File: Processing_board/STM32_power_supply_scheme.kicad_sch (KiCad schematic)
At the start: 14 parts

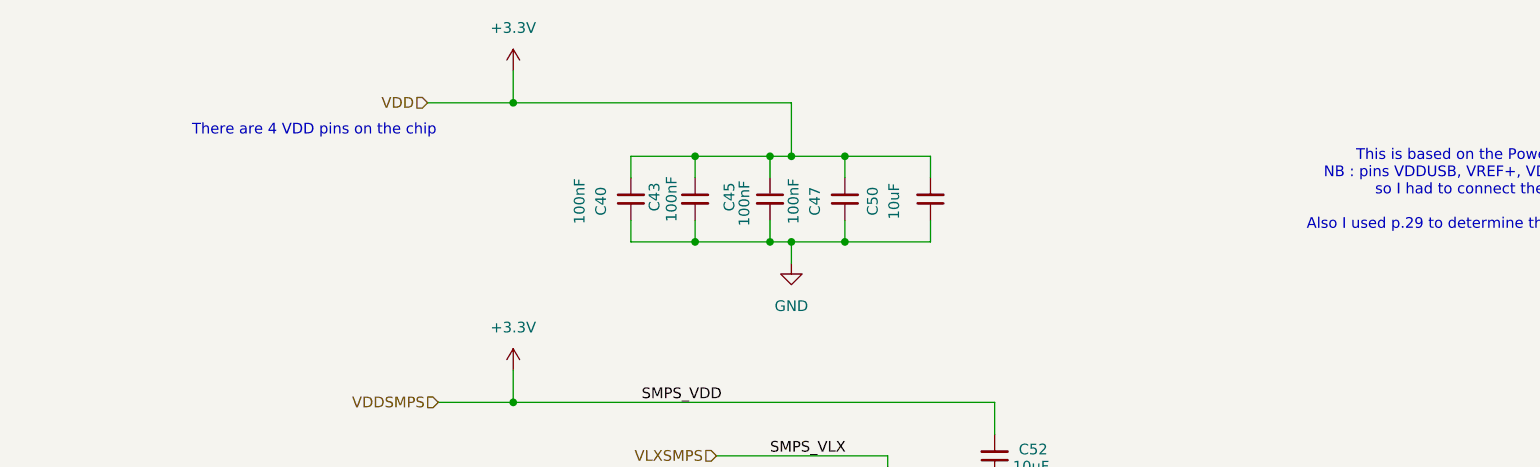
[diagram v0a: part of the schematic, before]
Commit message: created BOM, deleted useless folder Components and renamed CAD_Models to Parts
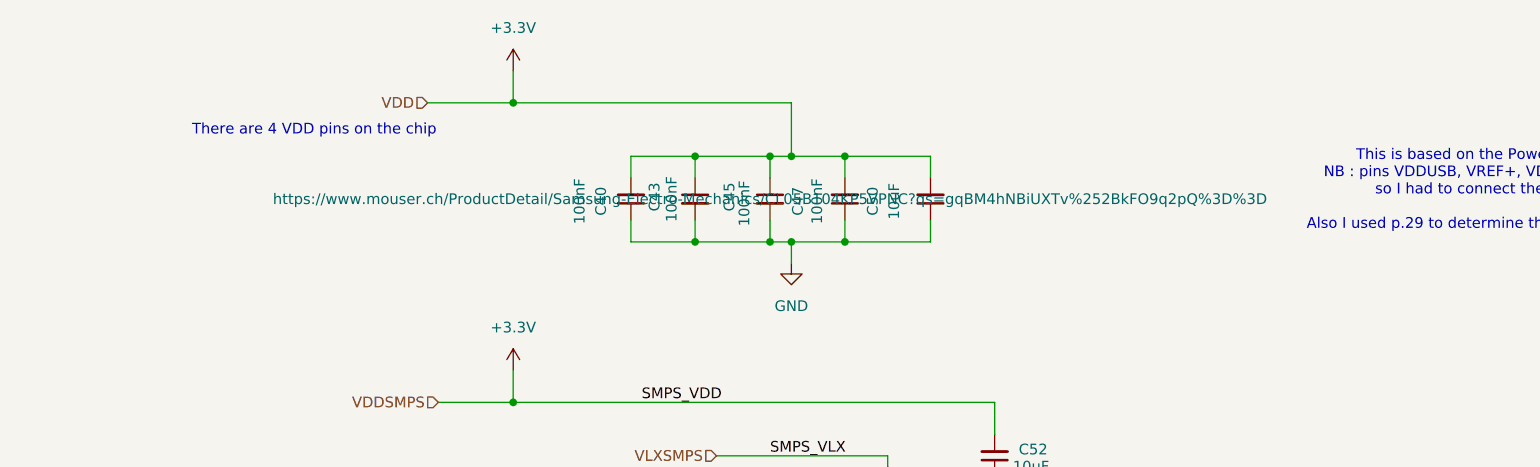
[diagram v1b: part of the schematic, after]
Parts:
- C40, C41, C42, C43, C45, C46, C47, C51: Link (none) -> https://www.mouser.ch/ProductDetail/Samsung-Electro-Mechani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; MANUFACTURER (none) -> Samsung Electro-Mechanics; Manufacturer_Part_Number (none) -> CL05B104KP5VPNC; Panier (none) -> 1
- C44: Link (none) -> https://www.mouser.ch/ProductDetail/Samsung-Electro-Mechani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; MANUFACTURER (none) -> Samsung Electro-Mechanics; Manufacturer_Part_Number (none) -> CL05A105KP5NNNC; Panier (none) -> 1
- C48: Link (none) -> https://www.mouser.ch/ProductDetail/KEMET/C0402C473K8RACAUT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; MANUFACTURER (none) -> KEMET; Manufacturer_Part_Number (none) -> C0402C473K8RACAUTO7411; Panier (none) -> 1
- C49: Link (none) -> https://www.mouser.ch/ProductDetail/YAGEO/CC0402KRX5R6BB475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; MANUFACTURER (none) -> YAGEO; Manufacturer_Part_Number (none) -> CC0402KRX5R6BB475; Panier (none) -> 1
- C50, C52: Link (none) -> https://www.mouser.ch/ProductDetail/Murata-Electronics/GRM1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; MANUFACTURER (none) -> Murata Electronics; Manufacturer_Part_Number (none) -> GRM155R61A106ME11D; Panier (none) -> 1
- L3: Link (none) -> https://www.mouser.ch/ProductDetail/Wurth-Elektronik/744797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; MANUFACTURER (none) -> Wurth Elektronik; Manufacturer_Part_Number (none) -> 74479774222; Panier (none) -> 1

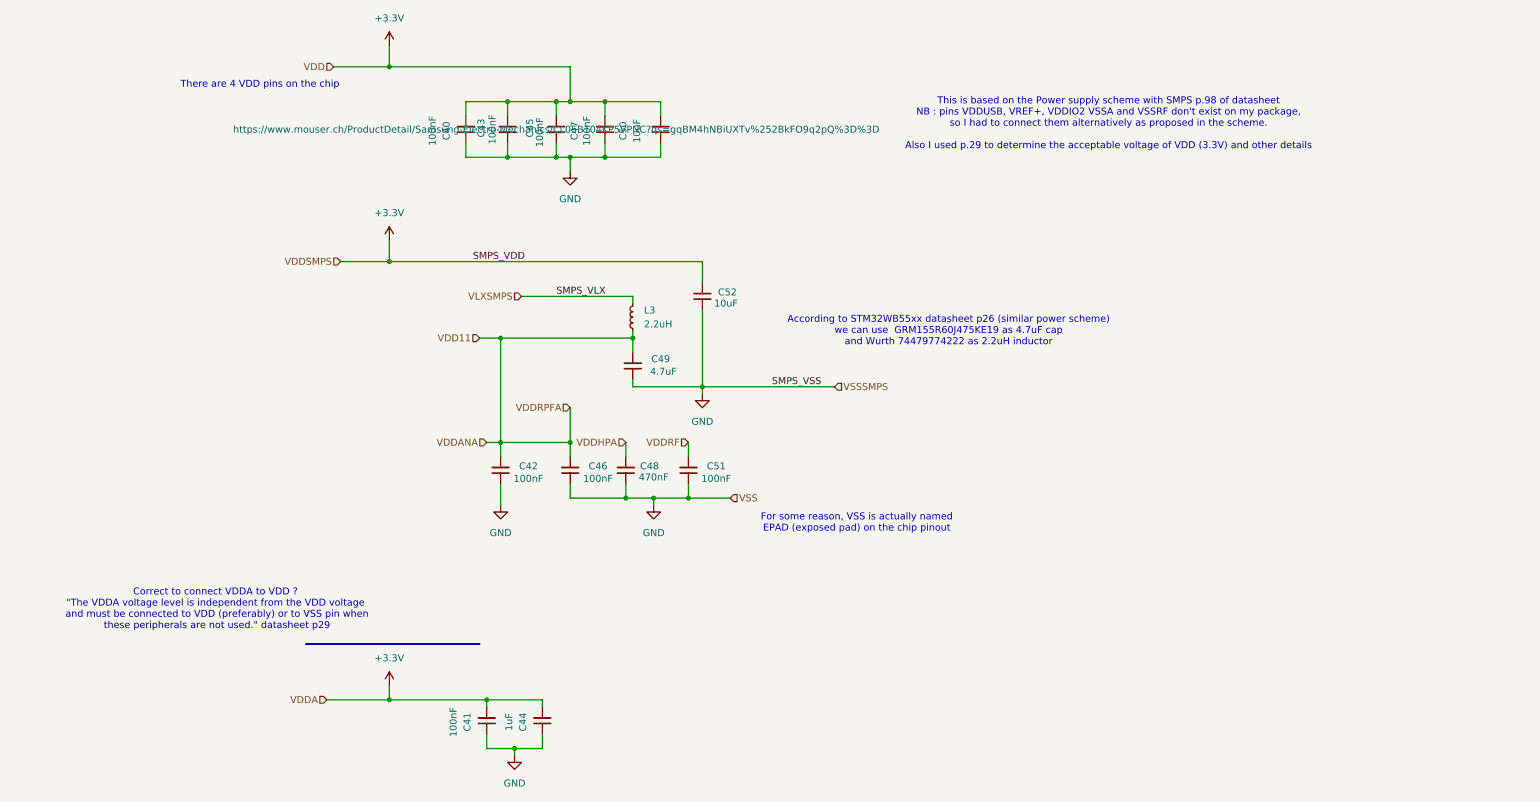
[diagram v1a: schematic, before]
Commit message: added N-Pulse logo etc, added open jumper solder bridge between pins VDD11 and VDDRFPA just in case
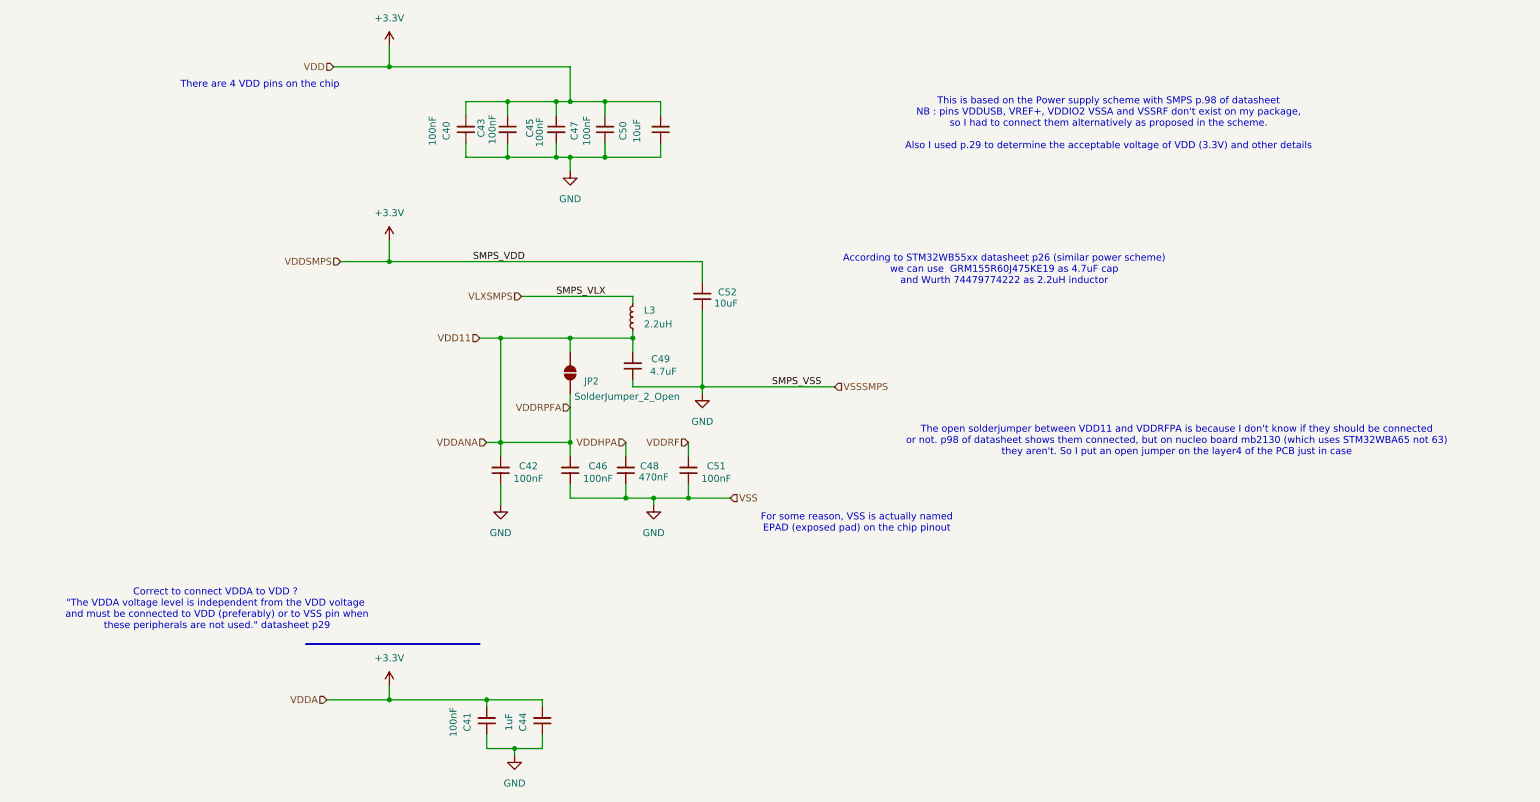
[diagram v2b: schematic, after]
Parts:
- added JP2: SolderJumper_2_Open, Jumper:SolderJumper-2_P1.3mm_Open_RoundedPad1.0x1.5mm, symbol Jumper:SolderJumper_2_Open
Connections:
- net VDD11: now also JP2.1 (A), JP2.2 (B)
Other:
- note added: "The open solderjumper between VDD11 and VDDRFPA is because I don't know if they should be connected or not. p98 of datasheet shows them connected, but on nucleo board mb2130 (which uses STM32WBA65 not 63) they aren't. So I put an open jumper on the layer4 of the PCB just in case"
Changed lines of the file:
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@@
+		)
+	)
+	(text "The open solderjumper between VDD11 and VDDRFPA is because I don't know if they should be connected\nor not. p98 of datasheet shows them connected, but on nucleo board mb2130 (which uses STM32WBA65 not 63)\nthey aren't. So I put an open jumper on the layer4 of the PCB just in case"
+		(exclude_from_sim no)
+		(at 227.584 96.266 0)
+		(effects
+			(font
+				(size 1.27 1.27)
+			)
 		)
 	)
@@
 	(text "According to STM32WB55xx datasheet p26 (similar power scheme)\nwe can use  GRM155R60J475KE19 as 4.7uF cap\nand Wurth 74479774222 as 2.2uH inductor"
 		(exclude_from_sim no)
-		(at 185.928 76.2 0)
+		(at 196.088 65.024 0)
 		(effects
 			(font
@@
 	)
 	(junction
+		(at 116.84 77.47)
+		(diameter 0)
+		(color 0 0 0 0)
+	)
+	(junction
 		(at 128.27 77.47)
 		(diameter 0)
@@
 	(wire
 		(pts
+			(xy 116.84 77.47) (xy 116.84 80.01)
+		)
+		(stroke
+			(width 0)
+			(type default)
+		)
+	)
+	(wire
+		(pts
 			(xy 116.84 96.52) (xy 116.84 99.06)
 		)
@@
 	(wire
 		(pts
+			(xy 116.84 77.47) (xy 128.27 77.47)
+		)
+		(stroke
+			(width 0)
+			(type default)
+		)
+	)
+	(wire
+		(pts
 			(xy 72.39 143.51) (xy 83.82 143.51)
 		)
@@
 	(wire
 		(pts
-			(xy 104.14 77.47) (xy 128.27 77.47)
+			(xy 104.14 77.47) (xy 116.84 77.47)
 		)
 		(stroke
@@
 	(wire
 		(pts
-			(xy 116.84 90.17) (xy 116.84 96.52)
+			(xy 116.84 87.63) (xy 116.84 96.52)
 		)
 		(stroke
@@
 					(size 1.27 1.27)
 				)
+				(hide yes)
 			)
 		)
@@
 					(unit 1)
 				)
+			)
+		)
+	)
+	(symbol
+		(lib_id "Jumper:SolderJumper_2_Open")
+		(at 116.84 83.82 270)
+		(unit 1)
+		(exclude_from_sim yes)
+		(in_bom no)
+		(on_board yes)
+		(dnp no)
+		(property "Reference" "JP2"
+			(at 119.38 85.344 90)
+			(effects
+				(font
+					(size 1.27 1.27)
+				)
+				(justify left)
+			)
+		)
+		(property "Value" "SolderJumper_2_Open"
+			(at 117.602 88.138 90)
+			(effects
+				(font
+					(size 1.27 1.27)
+				)
+				(justify left)
+			)
+		)
+		(property "Footprint" "Jumper:SolderJumper-2_P1.3mm_Open_RoundedPad1.0x1.5mm"
+			(at 116.84 83.82 0)
+			(effects
+				(font
+					(size 1.27 1.27)
+				)
+				(hide yes)
+			)
+		)
+		(property "Datasheet" "~"
+			(at 116.84 83.82 0)
+			(effects
+				(font
+					(size 1.27 1.27)
+				)
+				(hide yes)
+			)
+		)
+		(property "Description" "Solder Jumper, 2-pole, open"
+			(at 116.84 83.82 0)
+			(effects
+				(font
+					(size 1.27 1.27)
+				)
+				(hide yes)
+			)
+		)
+		(pin "1"
+		)
+		(pin "2"
+		)
+		(instances
+			(project ""
+				(path "/b48cfd4a-6c36-4270-b2b4-45cb26e35477/5bac6806-0b59-49c1-a3ef-3d4674d750e6"
+					(reference "JP2")
+					(unit 1)
+				)

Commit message: added Block Diagram (in KiCad and PDF) ; minor silkscreen cleanup
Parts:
- C40, C41, C42, C43, C45, C46, C47, C51: Link https://www.mouser.ch/ProductDetail/Samsung-Electro-Mechani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 -> https://eu.mouser.com/ProductDetail/Samsung-Electro-Mechani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; Manufacturer_Part_Number CL05B104KP5VPNC -> CL05B104KP5VPNC
- C49: Link https://www.mouser.ch/ProductDetail/YAGEO/CC0402KRX5R6BB475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 -> https://www.digikey.ch/en/products/detail/murata-electronic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; MANUFACTURER YAGEO -> Murata Electronics; Manufacturer_Part_Number CC0402KRX5R6BB475 -> GRM155C61E475ME15D
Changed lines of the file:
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@@
 			)
 		)
-		(property "Link" "https://www.mouser.ch/ProductDetail/Samsung-Electro-Mechanics/CL05B104KP5VPNC?qs=gqBM4hNBiUXTv%252BkFO9q2pQ%3D%3D"
+		(property "Link" "https://eu.mouser.com/ProductDetail/Samsung-Electro-Mechanics/CL05B104KP5VPNC?qs=gqBM4hNBiUXTv%252BkFO9q2pQ%3D%3D"
 			(at 138.43 101.6 0)
 			(effects
@@
 			)
 		)
-		(property "Manufacturer_Part_Number" "CL05B104KP5VPNC"
+		(property "Manufacturer_Part_Number" "CL05B104KP5VPNC "
 			(at 138.43 101.6 0)
 			(effects
@@
 			)
 		)
-		(property "Link" "https://www.mouser.ch/ProductDetail/Samsung-Electro-Mechanics/CL05B104KP5VPNC?qs=gqBM4hNBiUXTv%252BkFO9q2pQ%3D%3D"
+		(property "Link" "https://eu.mouser.com/ProductDetail/Samsung-Electro-Mechanics/CL05B104KP5VPNC?qs=gqBM4hNBiUXTv%252BkFO9q2pQ%3D%3D"
 			(at 123.19 39.37 0)
 			(effects
@@
 			)
 		)
-		(property "Manufacturer_Part_Number" "CL05B104KP5VPNC"
+		(property "Manufacturer_Part_Number" "CL05B104KP5VPNC "
 			(at 123.19 39.37 0)
 			(effects
@@
 			)
 		)
-		(property "Link" "https://www.mouser.ch/ProductDetail/Samsung-Electro-Mechanics/CL05B104KP5VPNC?qs=gqBM4hNBiUXTv%252BkFO9q2pQ%3D%3D"
+		(property "Link" "https://eu.mouser.com/ProductDetail/Samsung-Electro-Mechanics/CL05B104KP5VPNC?qs=gqBM4hNBiUXTv%252BkFO9q2pQ%3D%3D"
 			(at 114.3 39.37 0)
 			(effects
@@
 			)
 		)
-		(property "Manufacturer_Part_Number" "CL05B104KP5VPNC"
+		(property "Manufacturer_Part_Number" "CL05B104KP5VPNC "
 			(at 114.3 39.37 0)
 			(effects
@@
 			)
 		)
-		(property "Link" "https://www.mouser.ch/ProductDetail/YAGEO/CC0402KRX5R6BB475?qs=tS%2FAHvPQ%2F57yk%252BaeAkyovA%3D%3D"
+		(property "Link" "https://www.digikey.ch/en/products/detail/murata-electronics/GRM155C61E475ME15D/16821133"
 			(at 128.27 82.55 0)
 			(effects
@@
 			)
 		)
-		(property "MANUFACTURER" "YAGEO"
+		(property "MANUFACTURER" "Murata Electronics"
 			(at 128.27 82.55 0)
 			(effects
@@
 			)
 		)
-		(property "Manufacturer_Part_Number" "CC0402KRX5R6BB475"
+		(property "Manufacturer_Part_Number" "GRM155C61E475ME15D"
 			(at 128.27 82.55 0)
 			(effects
@@
 			)
 		)
-		(property "Link" "https://www.mouser.ch/ProductDetail/Samsung-Electro-Mechanics/CL05B104KP5VPNC?qs=gqBM4hNBiUXTv%252BkFO9q2pQ%3D%3D"
+		(property "Link" "https://eu.mouser.com/ProductDetail/Samsung-Electro-Mechanics/CL05B104KP5VPNC?qs=gqBM4hNBiUXTv%252BkFO9q2pQ%3D%3D"
 			(at 104.14 101.6 0)
 			(effects
@@
 			)
 		)
-		(property "Manufacturer_Part_Number" "CL05B104KP5VPNC"
+		(property "Manufacturer_Part_Number" "CL05B104KP5VPNC "
 			(at 104.14 101.6 0)
 			(effects
@@
 			)
 		)
-		(property "Link" "https://www.mouser.ch/ProductDetail/Samsung-Electro-Mechanics/CL05B104KP5VPNC?qs=gqBM4hNBiUXTv%252BkFO9q2pQ%3D%3D"
+		(property "Link" "https://eu.mouser.com/ProductDetail/Samsung-Electro-Mechanics/CL05B104KP5VPNC?qs=gqBM4hNBiUXTv%252BkFO9q2pQ%3D%3D"
 			(at 97.79 39.37 0)
 			(effects
@@
 			)
 		)
-		(property "Manufacturer_Part_Number" "CL05B104KP5VPNC"
+		(property "Manufacturer_Part_Number" "CL05B104KP5VPNC "
 			(at 97.79 39.37 0)
 			(effects
@@
 			)
 		)
-		(property "Link" "https://www.mouser.ch/ProductDetail/Samsung-Electro-Mechanics/CL05B104KP5VPNC?qs=gqBM4hNBiUXTv%252BkFO9q2pQ%3D%3D"
+		(property "Link" "https://eu.mouser.com/ProductDetail/Samsung-Electro-Mechanics/CL05B104KP5VPNC?qs=gqBM4hNBiUXTv%252BkFO9q2pQ%3D%3D"
 			(at 101.6 147.32 0)
 			(effects
@@
 			)
 		)
-		(property "Manufacturer_Part_Number" "CL05B104KP5VPNC"
+		(property "Manufacturer_Part_Number" "CL05B104KP5VPNC "
 			(at 101.6 147.32 0)
 			(effects
@@
 			)
 		)
-		(property "Link" "https://www.mouser.ch/ProductDetail/Samsung-Electro-Mechanics/CL05B104KP5VPNC?qs=gqBM4hNBiUXTv%252BkFO9q2pQ%3D%3D"
+		(property "Link" "https://eu.mouser.com/ProductDetail/Samsung-Electro-Mechanics/CL05B104KP5VPNC?qs=gqBM4hNBiUXTv%252BkFO9q2pQ%3D%3D"
 			(at 116.84 101.6 0)
 			(effects
@@
 			)
 		)
-		(property "Manufacturer_Part_Number" "CL05B104KP5VPNC"
+		(property "Manufacturer_Part_Number" "CL05B104KP5VPNC "
 			(at 116.84 101.6 0)
 			(effects
@@
 			)
 		)
-		(property "Link" "https://www.mouser.ch/ProductDetail/Samsung-Electro-Mechanics/CL05B104KP5VPNC?qs=gqBM4hNBiUXTv%252BkFO9q2pQ%3D%3D"
+		(property "Link" "https://eu.mouser.com/ProductDetail/Samsung-Electro-Mechanics/CL05B104KP5VPNC?qs=gqBM4hNBiUXTv%252BkFO9q2pQ%3D%3D"
 			(at 105.41 39.37 0)
 			(effects
@@
 			)
 		)
-		(property "Manufacturer_Part_Number" "CL05B104KP5VPNC"
+		(property "Manufacturer_Part_Number" "CL05B104KP5VPNC "
 			(at 105.41 39.37 0)
 			(effects
